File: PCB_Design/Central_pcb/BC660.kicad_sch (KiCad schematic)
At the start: 23 parts, among them J1 SIM8051-6-0-14-01-X-REVD, J1 SMA_CONNECTOR, J5 Conn_01x02_Pin, U2 BC660K-GL, U6 ESDS304DBVR

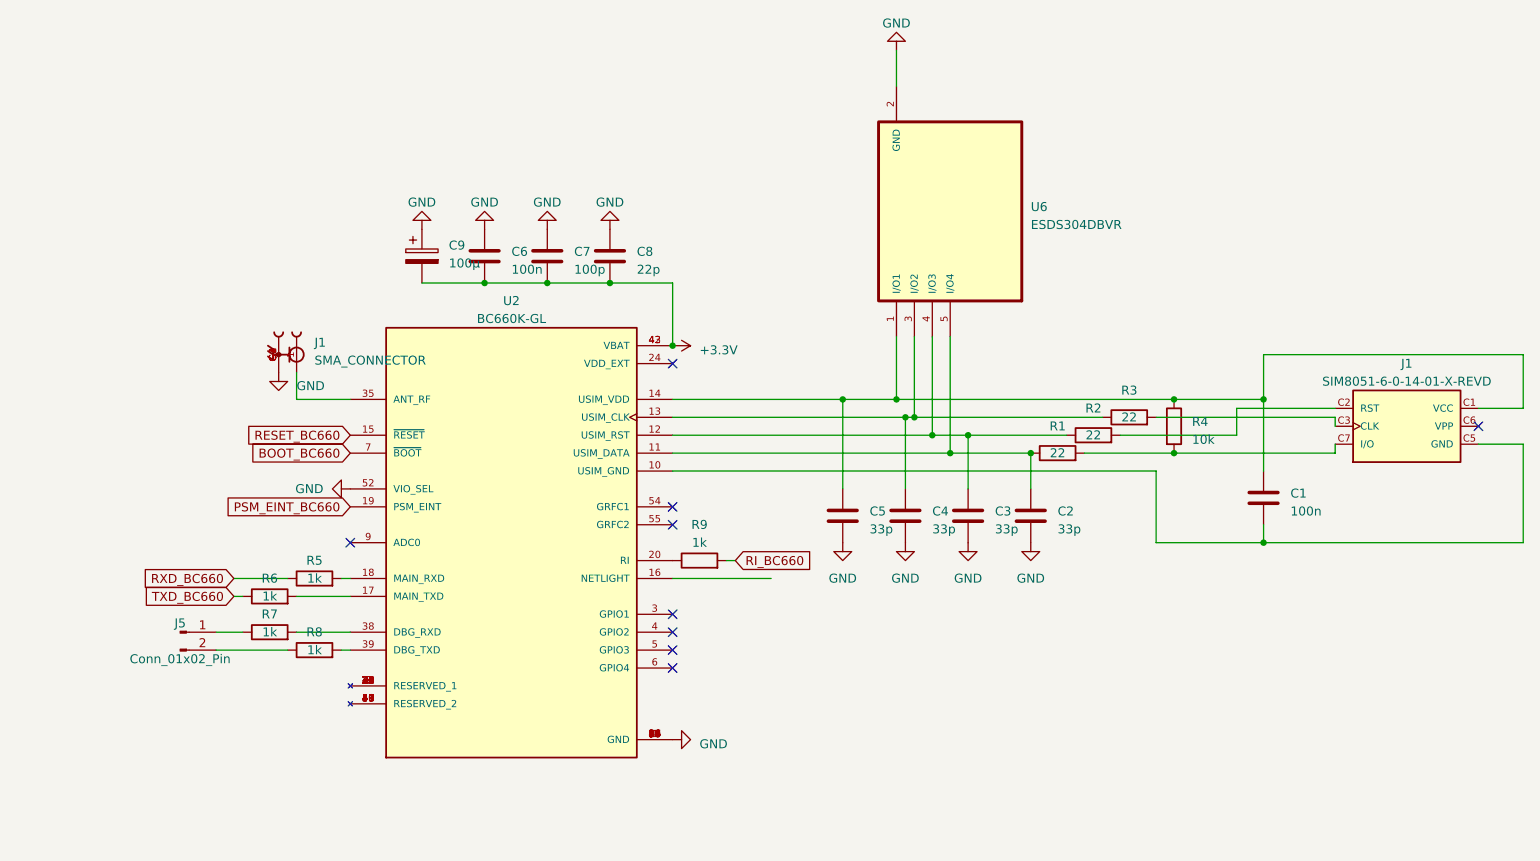
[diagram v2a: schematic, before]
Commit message: Initial PCB design
Rough sketch of what the layout could be
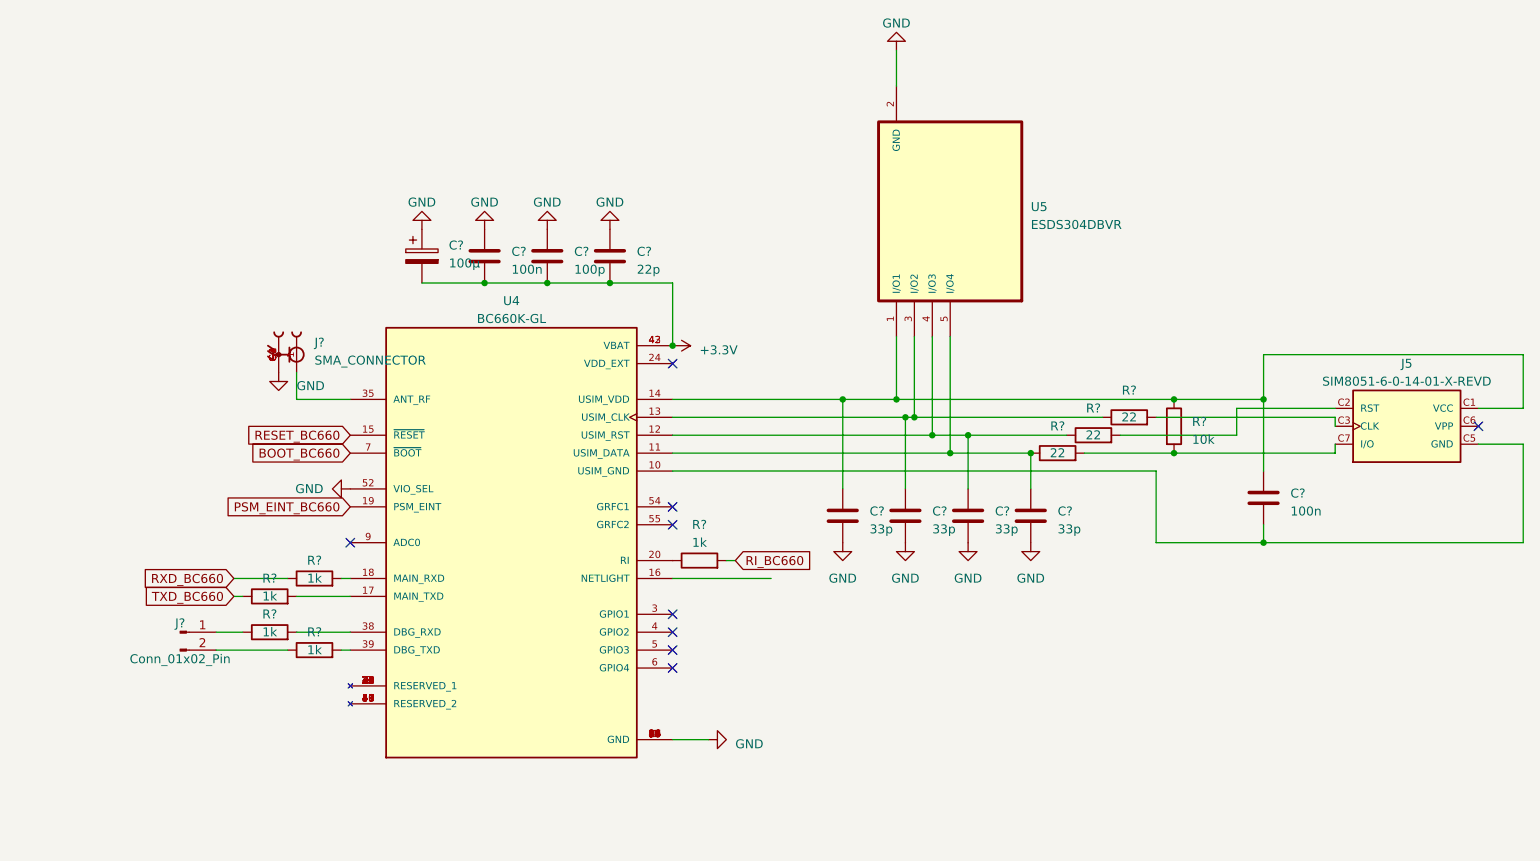
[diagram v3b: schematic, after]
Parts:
- renumbered C7 to C?, C5 to C?, C2 to C?, C9 to C?, C4 to C?, C3 to C?, C1 to C?, C8 to C?, C6 to C?, J1 to J5, J1 to J?, J5 to J?, R3 to R?, R4 to R?, R6 to R?, R7 to R?, R5 to R?, R1 to R?, R8 to R?, R9 to R?, R2 to R?, U2 to U4, U6 to U5

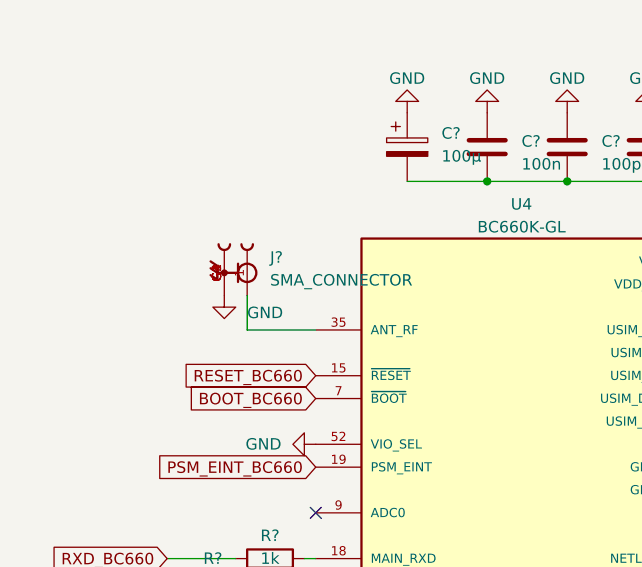
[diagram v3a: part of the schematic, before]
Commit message: PCB route
Volledig geroute nog juist controleren en mounting holes doen + controleren dat er overal gnd en 3.3v mooi verbonden is
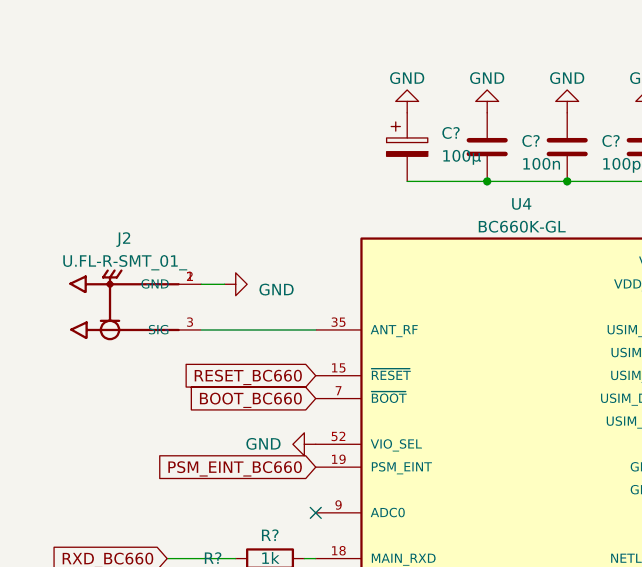
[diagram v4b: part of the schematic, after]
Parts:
- removed J?: SMA_CONNECTOR, Central:LPRS_SMA_CONNECTOR, symbol SMA_CONNECTOR:SMA_CONNECTOR
- added J2: U.FL-R-SMT_01_, Central:HRS_U.FL-R-SMT_01_, symbol UFL:U.FL-R-SMT_01_
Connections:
- net GND: now also J2.1 (GND), J2.2 (GND)
- net at U4.35 (ANT_RF): now also J2.3 (SIG)
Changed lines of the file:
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@@
+    (stroke (width 0) (type default))
+  )
+  (wire (pts (xy 74.93 77.47) (xy 77.47 77.47))
     (stroke (width 0) (type default))
   )
@@
     (stroke (width 0) (type default))
   )
-  (wire (pts (xy 80.01 78.74) (xy 80.01 82.55))
-    (stroke (width 0) (type default))
-  )
   (wire (pts (xy 170.18 87.63) (xy 175.26 87.63))
     (stroke (width 0) (type default))
@@
     (stroke (width 0) (type default))
   )
-  (wire (pts (xy 80.01 82.55) (xy 87.63 82.55))
+  (wire (pts (xy 74.93 82.55) (xy 87.63 82.55))
     (stroke (width 0) (type default))
   )
@@
     )
   )
+  (symbol (lib_id "power:GND") (at 77.47 77.47 90) (unit 1)
+    (in_bom yes) (on_board yes) (dnp no) (fields_autoplaced)
+    (property "Reference" "#PWR025" (at 83.82 77.47 0)
+      (effects (font (size 1.27 1.27)) hide)
+    )
+    (property "Value" "GND" (at 81.28 78.105 90)
+      (effects (font (size 1.27 1.27)) (justify right))
+    )
+    (property "Footprint" "" (at 77.47 77.47 0)
+      (effects (font (size 1.27 1.27)) hide)
+    )
+    (property "Datasheet" "" (at 77.47 77.47 0)
+      (effects (font (size 1.27 1.27)) hide)
+    )
+    (pin "1")
+    (instances
+      (project "Central_pcb"
+        (path "/4d244925-fc91-48ed-8daa-e4f0d6afeb7f/a01f4f1b-67d6-4452-bfd1-ae36b9ad65e8"
+          (reference "#PWR025") (unit 1)
+        )
+      )
+    )
+  )
   (symbol (lib_id "Device:R") (at 198.12 85.09 90) (unit 1)
     (in_bom yes) (on_board yes) (dnp no)
@@
         (path "/d627ecd8-d3ea-468a-86f8-a115d49eee0e"
           (reference "#PWR?") (unit 1)
-        )
-      )
-    )
-  )
-  (symbol (lib_id "SMA_CONNECTOR:SMA_CONNECTOR") (at 80.01 76.2 270) (unit 1)
-    (in_bom yes) (on_board yes) (dnp no) (fields_autoplaced)
-    (property "Reference" "J?" (at 82.55 74.4855 90)
-      (effects (font (size 1.27 1.27)) (justify left))
-    )
-    (property "Value" "SMA_CONNECTOR" (at 82.55 77.0255 90)
-      (effects (font (size 1.27 1.27)) (justify left))
-    )
-    (property "Footprint" "Central:LPRS_SMA_CONNECTOR" (at 80.01 76.2 0)
-      (effects (font (size 1.27 1.27)) (justify bottom) hide)
-    )
-    (property "Datasheet" "" (at 80.01 76.2 0)
-      (effects (font (size 1.27 1.27)) hide)
-    )
-    (property "MF" "LPRS" (at 80.01 76.2 0)
-      (effects (font (size 1.27 1.27)) (justify bottom) hide)
-    )
-    (property "MAXIMUM_PACKAGE_HEIGHT" "8.3 mm" (at 80.01 76.2 0)
-      (effects (font (size 1.27 1.27)) (justify bottom) hide)
-    )
-    (property "Package" "None" (at 80.01 76.2 0)
-      (effects (font (size 1.27 1.27)) (justify bottom) hide)
-    )
-    (property "Price" "None" (at 80.01 76.2 0)
-      (effects (font (size 1.27 1.27)) (justify bottom) hide)
-    )
-    (property "Check_prices" "https://www.snapeda.com/parts/SMA%20CONNECTOR/LPRS/view-part/?ref=eda" (at 80.01 76.2 0)
-      (effects (font (size 1.27 1.27)) (justify bottom) hide)
-    )
-    (property "STANDARD" "Manufacturer Recommendations" (at 80.01 76.2 0)
-      (effects (font (size 1.27 1.27)) (justify bottom) hide)
-    )
-    (property "PARTREV" "1.3" (at 80.01 76.2 0)
-      (effects (font (size 1.27 1.27)) (justify bottom) hide)
-    )
-    (property "SnapEDA_Link" "https://www.snapeda.com/parts/SMA%20CONNECTOR/LPRS/view-part/?ref=snap" (at 80.01 76.2 0)
-      (effects (font (size 1.27 1.27)) (justify bottom) hide)
-    )
-    (property "MP" "SMA CONNECTOR" (at 80.01 76.2 0)
-      (effects (font (size 1.27 1.27)) (justify bottom) hide)
-    )
-    (property "Description" "\nRF Coaxial Straight SMA Connector\n" (at 80.01 76.2 0)
-      (effects (font (size 1.27 1.27)) (justify bottom) hide)
-    )
-    (property "Availability" "In Stock" (at 80.01 76.2 0)
-      (effects (font (size 1.27 1.27)) (justify bottom) hide)
-    )
-    (property "MANUFACTURER" "LPRS" (at 80.01 76.2 0)
-      (effects (font (size 1.27 1.27)) (justify bottom) hide)
-    )
-    (pin "1")
-    (pin "G1")
-    (pin "G2")
-    (pin "G3")
-    (pin "G4")
-    (instances
-      (project "Central_pcb"
-        (path "/4d244925-fc91-48ed-8daa-e4f0d6afeb7f"
-          (reference "J?") (unit 1)
-        )
-        (path "/4d244925-fc91-48ed-8daa-e4f0d6afeb7f/a01f4f1b-67d6-4452-bfd1-ae36b9ad65e8"
-          (reference "J4") (unit 1)
-        )
-      )
-      (project "bc660_breakoutboard"
-        (path "/d627ecd8-d3ea-468a-86f8-a115d49eee0e"
-          (reference "J?") (unit 1)
         )
       )
@@
     )
   )
+  (symbol (lib_id "UFL:U.FL-R-SMT_01_") (at 64.77 80.01 180) (unit 1)
+    (in_bom yes) (on_board yes) (dnp no) (fields_autoplaced)
+    (property "Reference" "J2" (at 66.38 72.39 0)
+      (effects (font (size 1.27 1.27)))
+    )
+    (property "Value" "U.FL-R-SMT_01_" (at 66.38 74.93 0)
+      (effects (font (size 1.27 1.27)))
+    )
+    (property "Footprint" "Central:HRS_U.FL-R-SMT_01_" (at 64.77 80.01 0)
+      (effects (font (size 1.27 1.27)) (justify bottom) hide)
+    )
+    (property "Datasheet" "" (at 64.77 80.01 0)
+      (effects (font (size 1.27 1.27)) hide)
+    )
+    (property "MF" "Hirose" (at 64.77 80.01 0)
+      (effects (font (size 1.27 1.27)) (justify bottom) hide)
+    )
+    (property "DESCRIPTION" "U.FL Series 6 Ghz 50 Ohm Ultra-small SMT Coaxial Cable Receptacle" (at 64.77 80.01 0)
+      (effects (font (size 1.27 1.27)) (justify bottom) hide)
+    )
+    (property "PACKAGE" "None" (at 64.77 80.01 0)
+      (effects (font (size 1.27 1.27)) (justify bottom) hide)
+    )
+    (property "PRICE" "0.84 USD" (at 64.77 80.01 0)
+      (effects (font (size 1.27 1.27)) (justify bottom) hide)
+    )
+    (property "Package" "None" (at 64.77 80.01 0)
+      (effects (font (size 1.27 1.27)) (justify bottom) hide)
+    )
+    (property "Check_prices" "https://www.snapeda.com/parts/U.FL-R-SMT(01)/Hirose+Electric+Co+Ltd/view-part/?ref=eda" (at 64.77 80.01 0)
+      (effects (font (size 1.27 1.27)) (justify bottom) hide)
+    )
+    (property "Price" "None" (at 64.77 80.01 0)
+      (effects (font (size 1.27 1.27)) (justify bottom) hide)
+    )
+    (property "SnapEDA_Link" "https://www.snapeda.com/parts/U.FL-R-SMT(01)/Hirose+Electric+Co+Ltd/view-part/?ref=snap" (at 64.77 80.01 0)
+      (effects (font (size 1.27 1.27)) (justify bottom) hide)
+    )
+    (property "MP" "U.FL-R-SMT(01)" (at 64.77 80.01 0)
+      (effects (font (size 1.27 1.27)) (justify bottom) hide)
+    )
+    (property "Purchase-URL" "https://www.snapeda.com/api/url_track_click_mouser/?unipart_id=49572&manufacturer=Hirose&part_name=U.FL-R-SMT(01)&search_term=None" (at 64.77 80.01 0)
+      (effects (font (size 1.27 1.27)) (justify bottom) hide)
+    )
+    (property "Availability" "In Stock" (at 64.77 80.01 0)
+      (effects (font (size 1.27 1.27)) (justify bottom) hide)
+    )
+    (property "AVAILABILITY" "Good" (at 64.77 80.01 0)
+      (effects (font (size 1.27 1.27)) (justify bottom) hide)
+    )
+    (property "Description" "\nU.FL (UMCC) Connector Receptacle, Male Pin 50Ohm Surface Mount Solder. RF Connectors / Coaxial Connectors\n" (at 64.77 80.01 0)
+      (effects (font (size 1.27 1.27)) (justify bottom) hide)
+    )
+    (pin "1")
+    (pin "2")
+    (pin "3")
+    (instances
+      (project "Central_pcb"
+        (path "/4d244925-fc91-48ed-8daa-e4f0d6afeb7f/a01f4f1b-67d6-4452-bfd1-ae36b9ad65e8"
+          (reference "J2") (unit 1)
+        )
+      )
+    )
+  )
   (symbol (lib_id "Device:R") (at 137.16 105.41 90) (unit 1)
     (in_bom yes) (on_board yes) (dnp no) (fields_autoplaced)
@@
         )
       )
-    )
-  )
-  (symbol (lib_id "power:GND") (at 77.47 78.74 0) (unit 1)
-    (in_bom yes) (on_board yes) (dnp no) (fields_autoplaced)
-    (property "Reference" "#PWR?" (at 77.47 85.09 0)
-      (effects (font (size 1.27 1.27)) hide)
-    )
-    (property "Value" "GND" (at 80.01 80.645 0)
-      (effects (font (size 1.27 1.27)) (justify left))
-    )
-    (property "Footprint" "" (at 77.47 78.74 0)
-      (effects (font (size 1.27 1.27)) hide)
-    )
-    (property "Datasheet" "" (at 77.47 78.74 0)
-      (effects (font (size 1.27 1.27)) hide)
-    )
-    (pin "1")
-    (instances
-      (project "Central_pcb"
-        (path "/4d244925-fc91-48ed-8daa-e4f0d6afeb7f"
-          (reference "#PWR?") (unit 1)
-        )
-        (path "/4d244925-fc91-48ed-8daa-e4f0d6afeb7f/a01f4f1b-67d6-4452-bfd1-ae36b9ad65e8"
-          (reference "#PWR025") (unit 1)
-        )
-      )
-      (project "bc660_breakoutboard"
-        (path "/d627ecd8-d3ea-468a-86f8-a115d49eee0e"
-          (reference "#PWR?") (unit 1)
-        )
-      )
